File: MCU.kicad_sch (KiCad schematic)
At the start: 10 parts, among them SW1 SW_MEC_5E, U1 STM32G050C8Tx

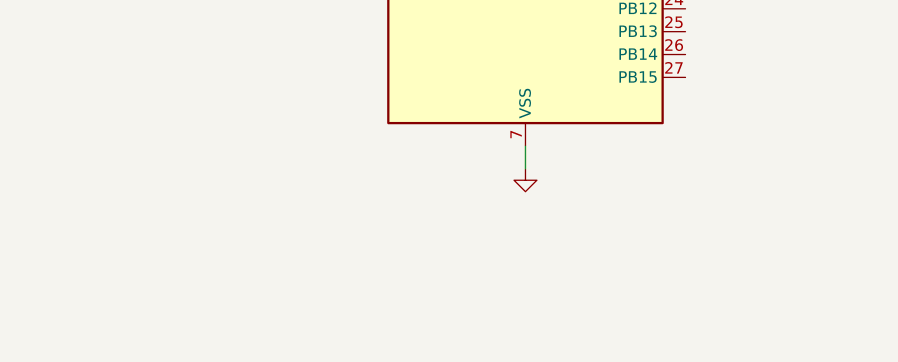
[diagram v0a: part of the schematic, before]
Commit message: Specefies which section is complete and incomplete
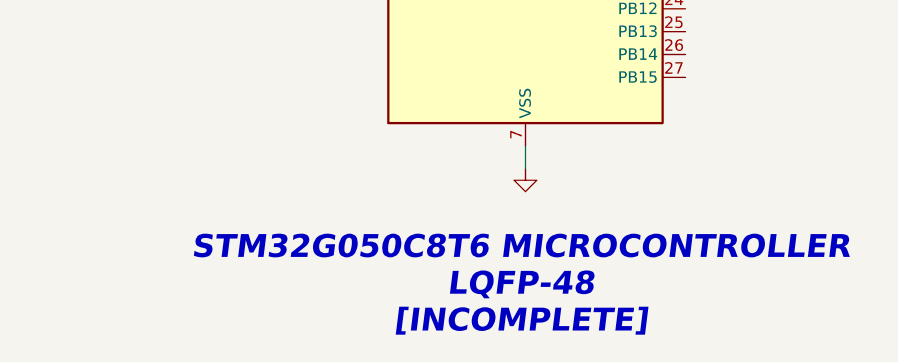
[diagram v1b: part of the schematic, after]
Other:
- note added: "STM32G050C8T6 MICROCONTROLLER LQFP-48 [INCOMPLETE]"
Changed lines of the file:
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@@
+		)
+	)
+	(text "STM32G050C8T6 MICROCONTROLLER\nLQFP-48\n[INCOMPLETE]"
+		(exclude_from_sim no)
+		(at 132.842 169.164 0)
+		(effects
+			(font
+				(face "Arial Black")
+				(size 2.54 2.54)
+				(thickness 0.254)
+				(bold yes)
+				(italic yes)
+				(color 0 193 255 1)
+			)
 		)
 	)
